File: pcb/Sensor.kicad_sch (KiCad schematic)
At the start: 60 parts, among them IC2 74HC14D-Q100,118, U2 OPA2376xxD

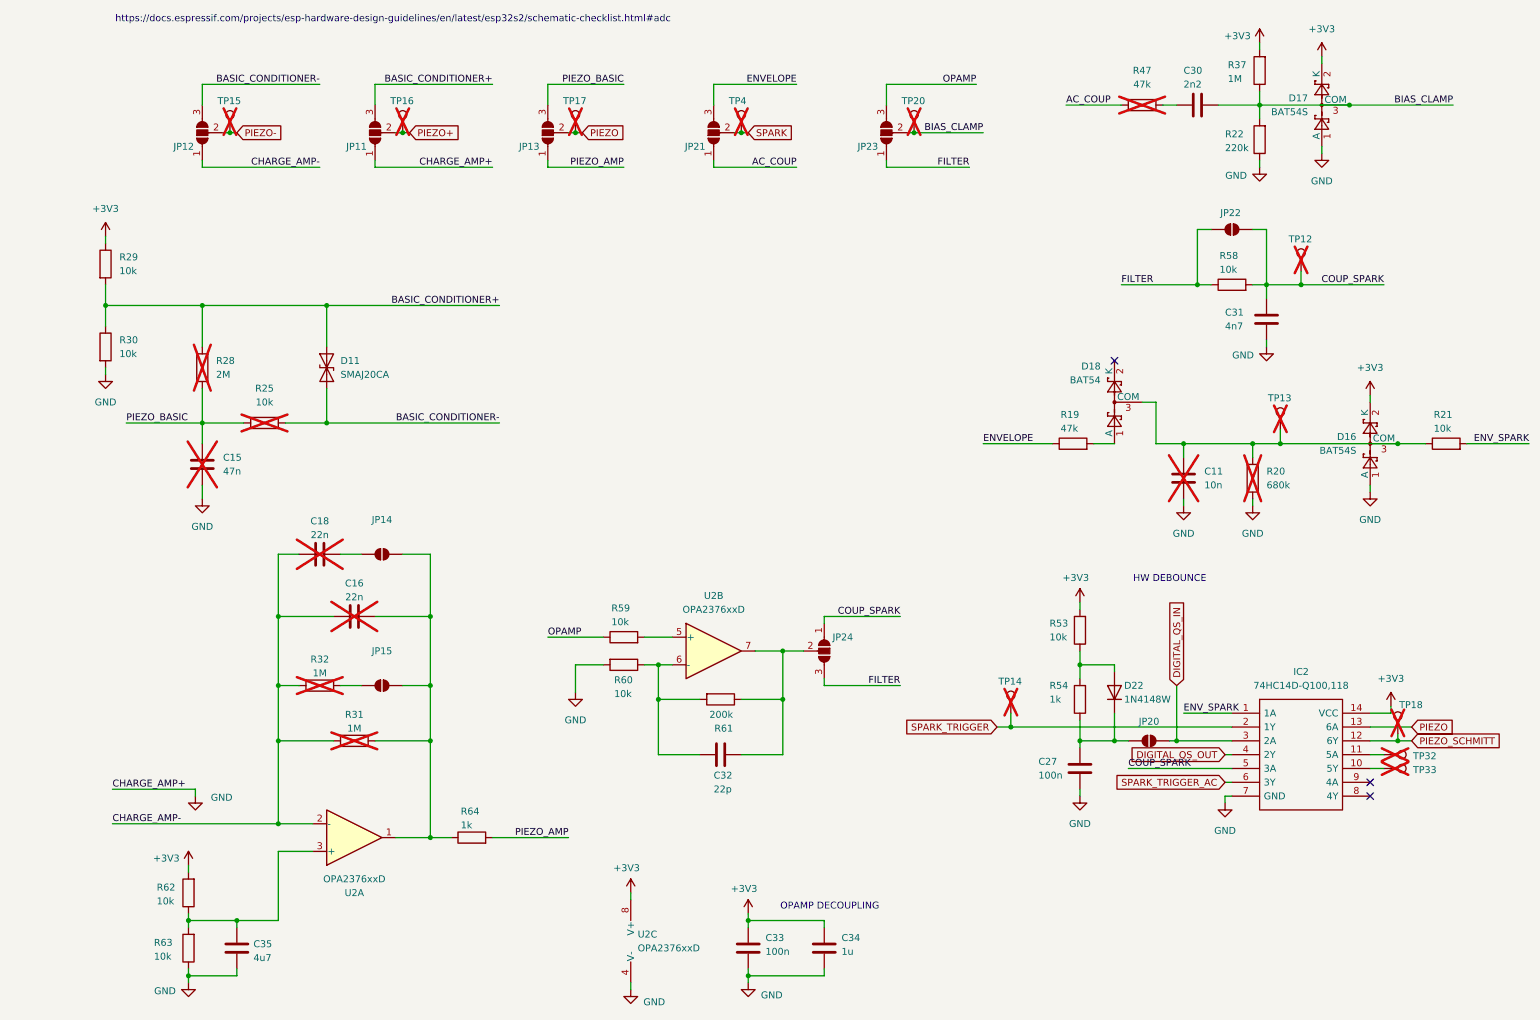
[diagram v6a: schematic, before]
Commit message: changed THT to SMD for both resistors and capacitors since they will be replaced by hand with soldering tweezers
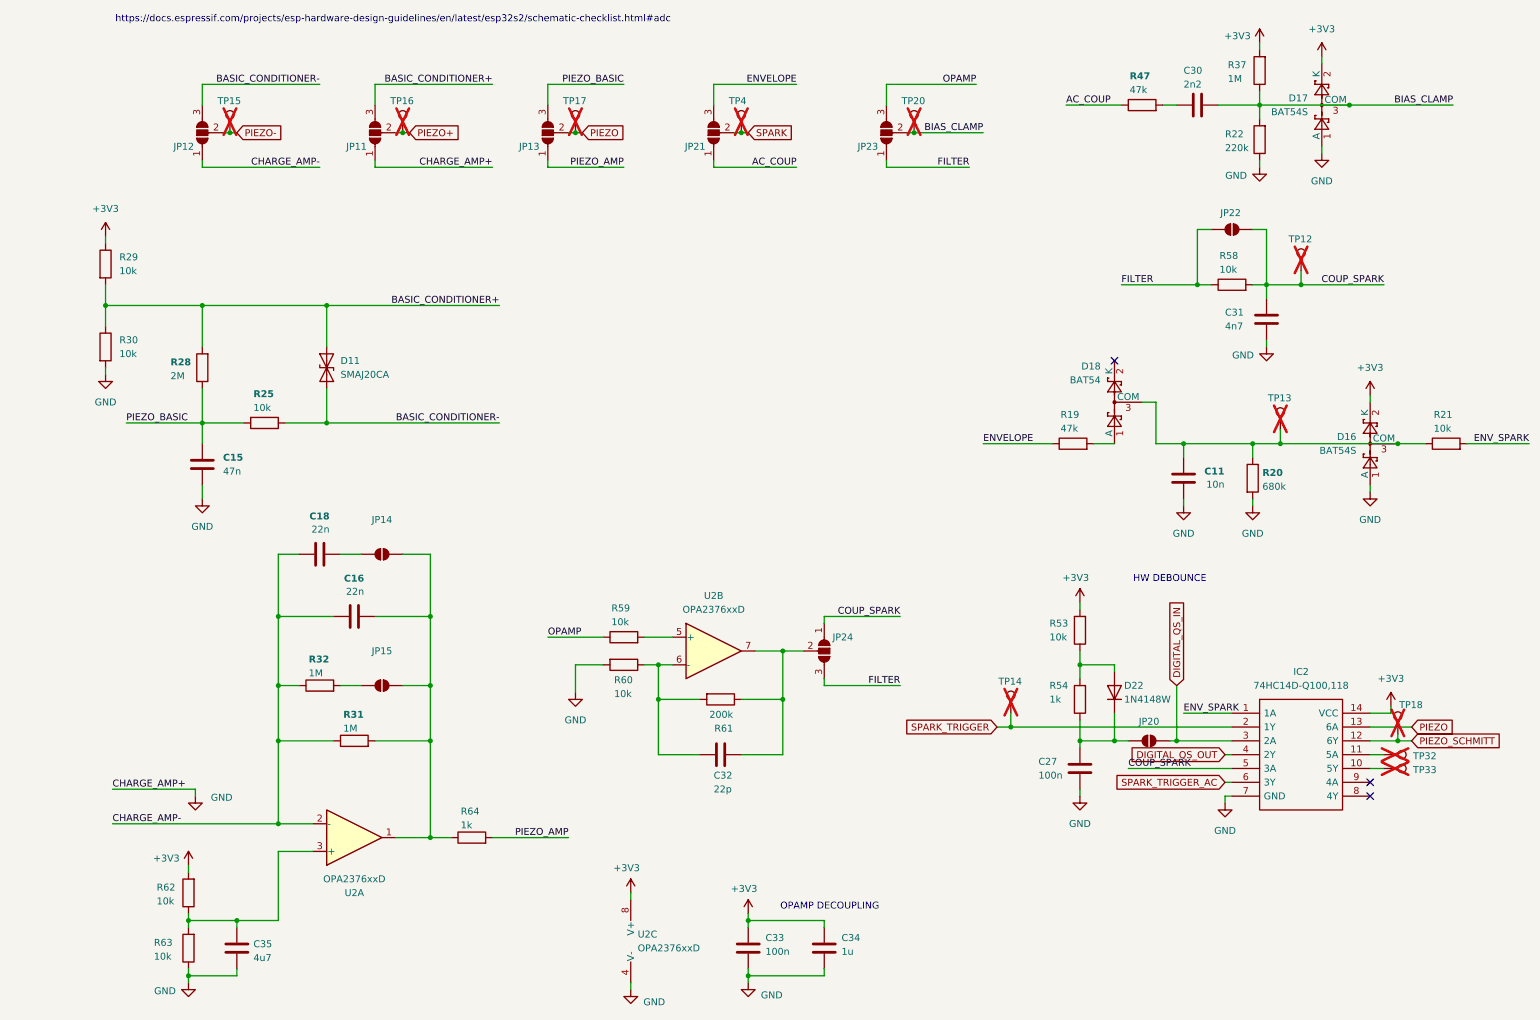
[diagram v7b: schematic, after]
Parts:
- C11, C15, C16, C18: footprint Capacitor_THT:C_Disc_D4.3mm_W1.9mm_P5.00mm -> Capacitor_SMD:C_0603_1608Metric; now fitted
- R20, R25, R28, R31, R32, R47: footprint Resistor_THT:R_Axial_DIN0204_L3.6mm_D1.6mm_P1.90mm_Vertical -> Resistor_SMD:R_0603_1608Metric; now fitted
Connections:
- net BASIC_CONDITIONER-: now also R25.1; no longer R25.2
- net GND: now also R20.2; no longer R20.1
- net PIEZO_BASIC: now also R25.2; no longer R25.1
- net at C11.1, D16.3 (COM), D18.3 (COM)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: now also R20.1; no longer R20.2

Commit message: revision 2.0: changed components numeration
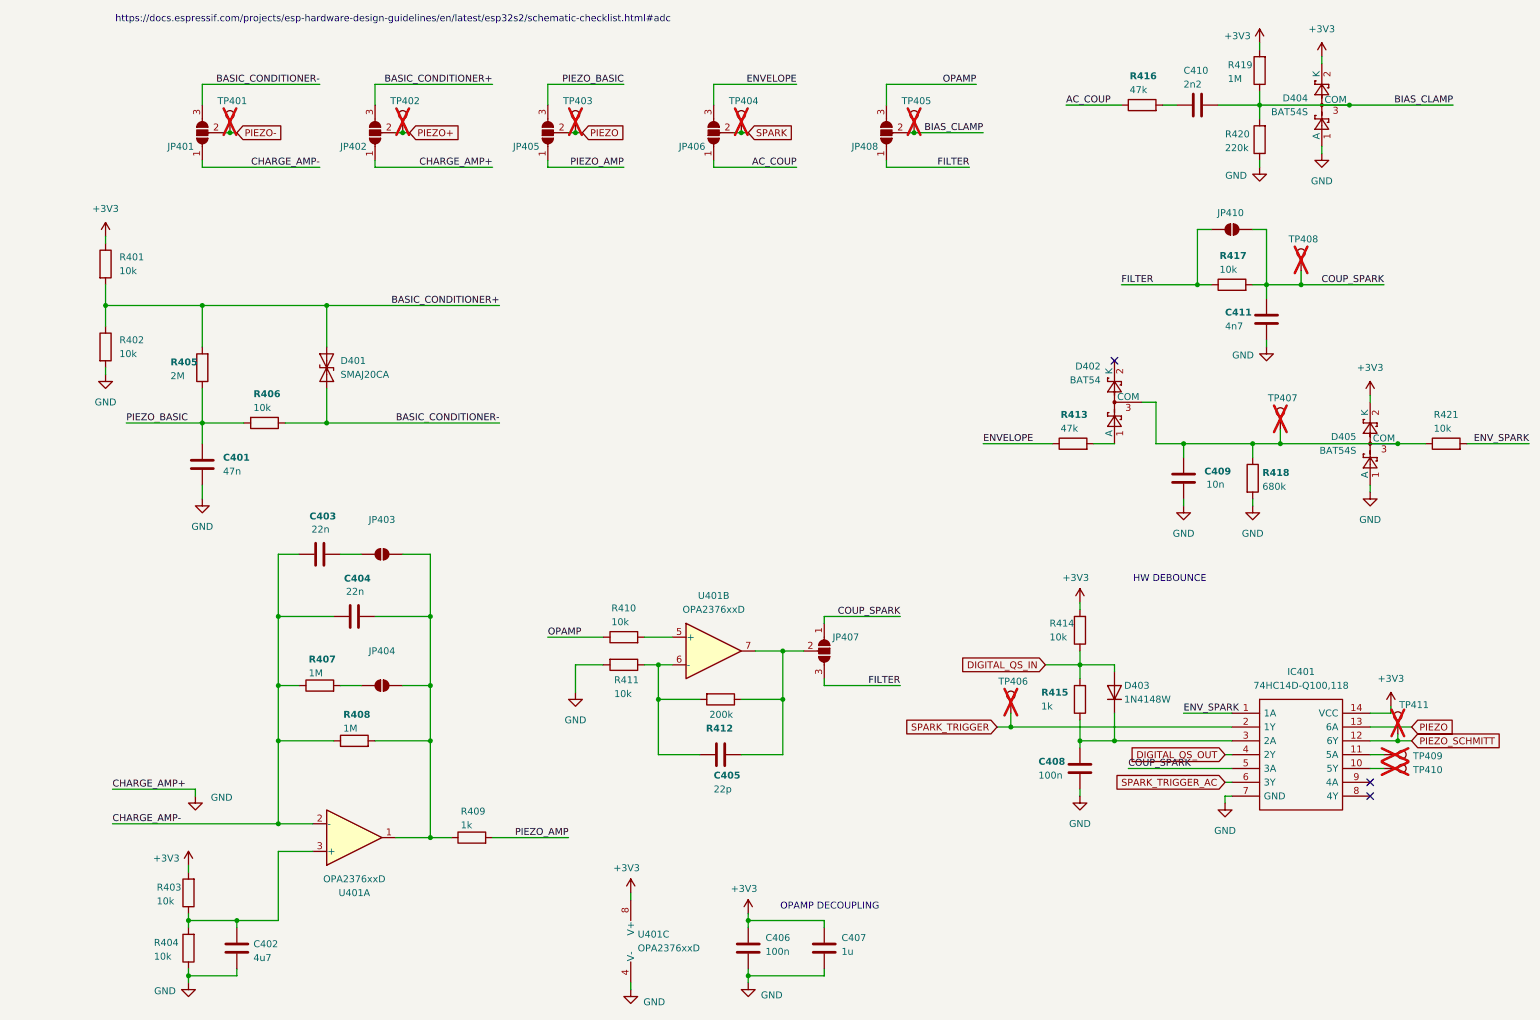
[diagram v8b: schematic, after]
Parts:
- removed JP20: SolderJumper_2_Open, Jumper:SolderJumper-2_P1.3mm_Open_RoundedPad1.0x1.5mm, symbol Jumper:SolderJumper_2_Open
- C401: renamed from C15; footprint Capacitor_SMD:C_0603_1608Metric -> Capacitor_SMD:C_0805_2012Metric
- C403: renamed from C18; footprint Capacitor_SMD:C_0603_1608Metric -> Capacitor_SMD:C_0805_2012Metric
- C404: renamed from C16; footprint Capacitor_SMD:C_0603_1608Metric -> Capacitor_SMD:C_0805_2012Metric
- C405: renamed from C32; footprint Capacitor_SMD:C_0603_1608Metric -> Capacitor_SMD:C_0805_2012Metric
- C408: renamed from C27; footprint Capacitor_SMD:C_0603_1608Metric -> Capacitor_SMD:C_0805_2012Metric
- C409: renamed from C11; footprint Capacitor_SMD:C_0603_1608Metric -> Capacitor_SMD:C_0805_2012Metric
- C411: renamed from C31; footprint Capacitor_SMD:C_0603_1608Metric -> Capacitor_SMD:C_0805_2012Metric
- R405: renamed from R28; footprint Resistor_SMD:R_0603_1608Metric -> Resistor_SMD:R_0805_2012Metric
- R406: renamed from R25; footprint Resistor_SMD:R_0603_1608Metric -> Resistor_SMD:R_0805_2012Metric
- R413: renamed from R19; footprint Resistor_SMD:R_0603_1608Metric -> Resistor_SMD:R_0805_2012Metric
- R415: renamed from R54; footprint Resistor_SMD:R_0603_1608Metric -> Resistor_SMD:R_0805_2012Metric
- R416: renamed from R47; footprint Resistor_SMD:R_0603_1608Metric -> Resistor_SMD:R_0805_2012Metric
- R417: renamed from R58; footprint Resistor_SMD:R_0603_1608Metric -> Resistor_SMD:R_0805_2012Metric
- R418: renamed from R20; footprint Resistor_SMD:R_0603_1608Metric -> Resistor_SMD:R_0805_2012Metric
- renumbered C35 to C402, C33 to C406, C34 to C407, C30 to C410, D11 to D401, D18 to D402, D22 to D403, D17 to D404, D16 to D405, IC2 to IC401, JP12 to JP401, JP11 to JP402, JP14 to JP403, JP15 to JP404, JP13 to JP405, JP21 to JP406, JP24 to JP407, JP23 to JP408, JP22 to JP410, R29 to R401, R30 to R402, R62 to R403, R63 to R404, R32 to R407, R31 to R408, R64 to R409, R59 to R410, R60 to R411, R61 to R412, R53 to R414, R37 to R419, R22 to R420, R21 to R421, TP15 to TP401, TP16 to TP402, TP17 to TP403, TP4 to TP404, TP20 to TP405, TP14 to TP406, TP13 to TP407, TP12 to TP408, TP32 to TP409, TP33 to TP410, TP18 to TP411, U2 to U401
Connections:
- net DIGITAL_QS_IN: now also D403.2 (A), R414.1, R415.2; no longer IC401.3 (2A)
- net at C408.2, D403.1 (K), R415.1: now also IC401.3 (2A)
